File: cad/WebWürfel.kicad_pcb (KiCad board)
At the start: 2 copper layers, 64 x 115 mm, 45 parts, among them K1 1x03, T1 IRF9952, T2 FDN337N, T3 IRLML9301, U1 WeMos_D1_mini, U2 TSR1-2450

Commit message: old led grid
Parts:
- added REF**: MountingHole_3.5mm, MountingHole:MountingHole_3.5mm, F.Cu at (117.5, 52.5)
- added REF**: MountingHole_3.5mm, MountingHole:MountingHole_3.5mm, F.Cu at (149.1, 52.5)
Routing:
- net GND: track 11.5 -> 13.6 mm
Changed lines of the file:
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@@
       (solder_mask_margin 0.1016) (thermal_bridge_angle 45))
+  )
+  (footprint "MountingHole:MountingHole_3.5mm" (layer "F.Cu")
+    (at 117.5 52.5)
+    (descr "Mounting Hole 3.5mm, no annular")
+    (tags "mounting hole 3.5mm no annular")
+    (attr exclude_from_pos_files exclude_from_bom)
+    (fp_text reference "REF**" (at 0 -4.5) (layer "F.SilkS")
+        (effects (font (size 1 1) (thickness 0.15)))
+    )
+    (fp_text value "MountingHole_3.5mm" (at 0 4.4) (layer "F.Fab") hide
+        (effects (font (size 1 1) (thickness 0.15)))
+    )
+    (fp_text user "${REFERENCE}" (at 0 0) (layer "F.Fab")
+        (effects (font (size 1 1) (thickness 0.15)))
+    )
+    (fp_circle (center 0 0) (end 3.5 0)
+      (stroke (width 0.15) (type solid)) (fill none) (layer "Cmts.User"))
+    (fp_circle (center 0 0) (end 3.75 0)
+      (stroke (width 0.05) (type solid)) (fill none) (layer "F.CrtYd"))
+    (pad "" np_thru_hole circle (at 0 0) (size 3.5 3.5) (drill 3.5) (layers "F&B.Cu" "*.Mask"))
   )
   (footprint "D1Mini_Wuerfel_aktuell:WS2812B_9" (layer "F.Cu")
@@
       (rotate (xyz 0 0 0))
     )
+  )
+  (footprint "MountingHole:MountingHole_3.5mm" (layer "F.Cu")
+    (at 149.1 52.5)
+    (descr "Mounting Hole 3.5mm, no annular")
+    (tags "mounting hole 3.5mm no annular")
+    (attr exclude_from_pos_files exclude_from_bom)
+    (fp_text reference "REF**" (at 0 -4.5) (layer "F.SilkS")
+        (effects (font (size 1 1) (thickness 0.15)))
+    )
+    (fp_text value "MountingHole_3.5mm" (at 0 4.5) (layer "F.Fab") hide
+        (effects (font (size 1 1) (thickness 0.15)))
+    )
+    (fp_text user "${REFERENCE}" (at 0 0) (layer "F.Fab")
+        (effects (font (size 1 1) (thickness 0.15)))
+    )
+    (fp_circle (center 0 0) (end 3.5 0)
+      (stroke (width 0.15) (type solid)) (fill none) (layer "Cmts.User"))
+    (fp_circle (center 0 0) (end 3.75 0)
+      (stroke (width 0.05) (type solid)) (fill none) (layer "F.CrtYd"))
+    (pad "" np_thru_hole circle (at 0 0) (size 3.5 3.5) (drill 3.5) (layers "*.Cu" "*.Mask"))
   )
   (footprint "D1Mini_Wuerfel_aktuell:WS2812B_9" (layer "F.Cu")
@@
     (pad "" np_thru_hole circle (at 0 0 180) (size 2.5 2.5) (drill 2.5) (layers "*.Cu" "*.Mask"))
   )
-  (gr_line (start 117.25 147.75) (end 117.25 150.75)
-    (stroke (width 0.4) (type default)) (layer "F.SilkS"))
-  (gr_line (start 122.75 138.25) (end 122.75 133.5)
-    (stroke (width 0.4) (type default)) (layer "F.SilkS"))
-  (gr_line (start 107.5 121.5) (end 107.5 127.25)
-    (stroke (width 1) (type default)) (layer "F.SilkS"))
-  (gr_line (start 134.75 135.5) (end 134.75 144)
-    (stroke (width 0.4) (type default)) (layer "F.SilkS"))
   (gr_line (start 101.29 155) (end 165.29 155)
     (stroke (width 0.3) (type solid)) (layer "Edge.Cuts"))
@@
   (gr_line (start 165.29 155) (end 165.29 40)
     (stroke (width 0.3) (type solid)) (layer "Edge.Cuts"))
+  (segment (start 108.458 112.014) (end 108.458 111.998) (width 2) (layer "F.Cu") (net 1))
   (segment (start 124.845 137.77) (end 125.365 137.25) (width 0.3) (layer "F.Cu") (net 1))
   (segment (start 128.25 137.25) (end 128.75 136.75) (width 0.3) (layer "F.Cu") (net 1))
   (segment (start 125.365 137.25) (end 128.25 137.25) (width 0.3) (layer "F.Cu") (net 1))
+  (segment (start 107 110.54) (end 108.458 111.998) (width 2) (layer "F.Cu") (net 1))
   (segment (start 124.845 139.2) (end 124.845 137.77) (width 0.3) (layer "F.Cu") (net 1))
   (via (at 107.5 127.25) (size 2) (drill 1.2) (layers "F.Cu" "B.Cu") (free) (net 1))
@@
   (zone (net 1) (net_name "GND") (layer "F.Cu") (name "GND_1") (hatch edge 0.5)
     (priority 2)
-    (connect_pads yes (clearance 0.5))
+    (connect_pads (clearance 0.5))
     (min_thickness 0.25) (filled_areas_thickness no)
     (fill yes (thermal_gap 0.5) (thermal_bridge_width 0.5) (smoothing fillet) (radius 1))
@@
         (xy 114.25 101.75)
         (xy 114.25 104)
-        (xy 160.5 104)
-        (xy 160.5 61.75)
+        (xy 158.95 104.013)
+        (xy 158.95 61.73)
       )
     )
@@
   (zone (net 1) (net_name "GND") (layer "F.Cu") (name "GND_0") (hatch edge 0.5)
     (priority 1)
-    (connect_pads yes (clearance 1.3))
+    (connect_pads (clearance 1.3))
     (min_thickness 0.25) (filled_areas_thickness no)
     (fill yes (thermal_gap 0.5) (thermal_bridge_width 0.5) (smoothing chamfer) (radius 1.3))
@@
       )
     )
+  )
+  (zone (net 1) (net_name "GND") (layer "F.Cu") (name "GND_3") (hatch edge 0.5)
+    (priority 3)
+    (connect_pads yes (clearance 1.3))
+    (min_thickness 0.25) (filled_areas_thickness no)
+    (fill yes (thermal_gap 0.5) (thermal_bridge_width 0.5) (smoothing chamfer) (radius 1.3))
+    (polygon
+      (pts
+        (xy 144.145 129.032)
+        (xy 144.145 130.175)
+        (xy 145.923 130.175)
+        (xy 145.923 129.032)
+      )
+    )
+  )
+  (zone (net 1) (net_name "GND") (layer "F.Cu") (name "GND4") (hatch edge 0.5)
+    (priority 3)
+    (connect_pads yes (clearance 1.3))
+    (min_thickness 0.25) (filled_areas_thickness no)
+    (fill yes (thermal_gap 0.5) (thermal_bridge_width 0.5))
+    (polygon
+      (pts
+        (xy 112.014 130.302)
+        (xy 112.014 132.08)
+        (xy 113.665 132.08)
+        (xy 113.665 130.302)
+      )
+    )

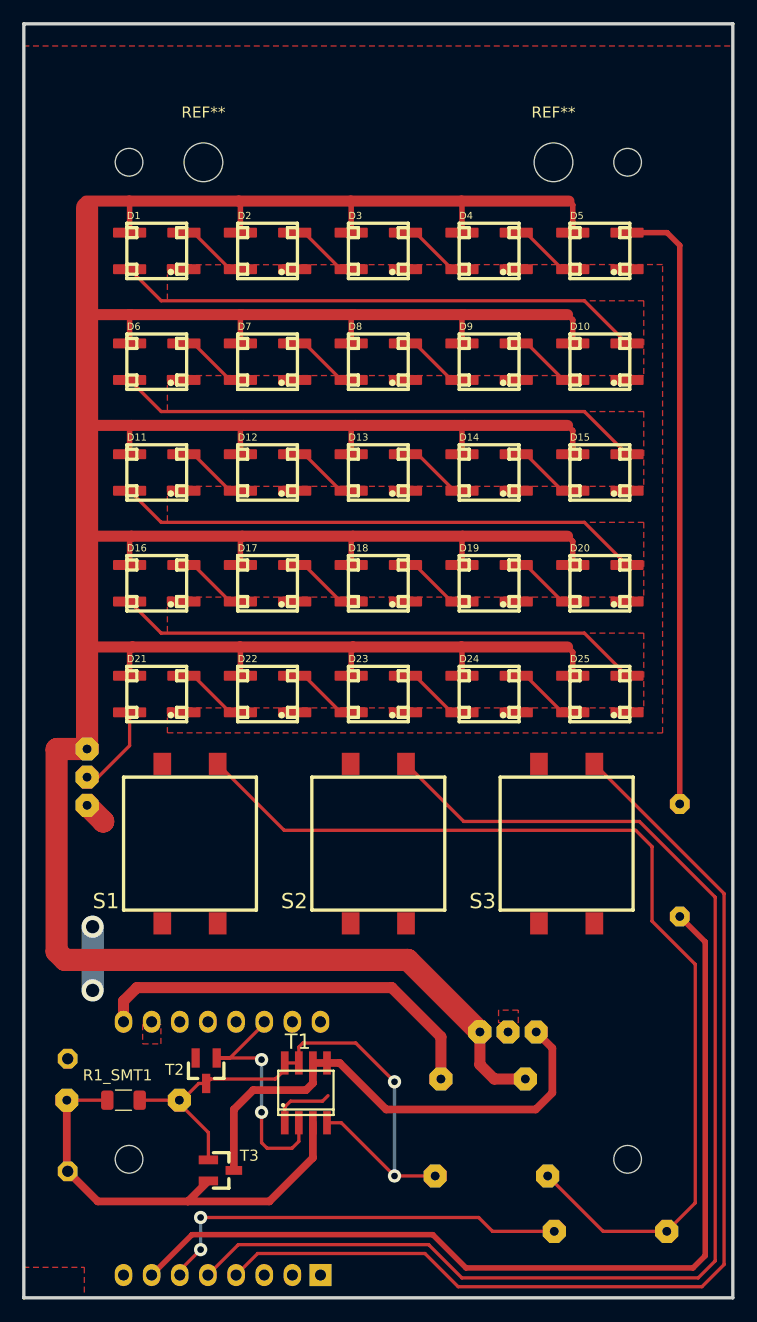
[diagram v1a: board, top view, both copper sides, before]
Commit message: rotated d1 mini by 90°
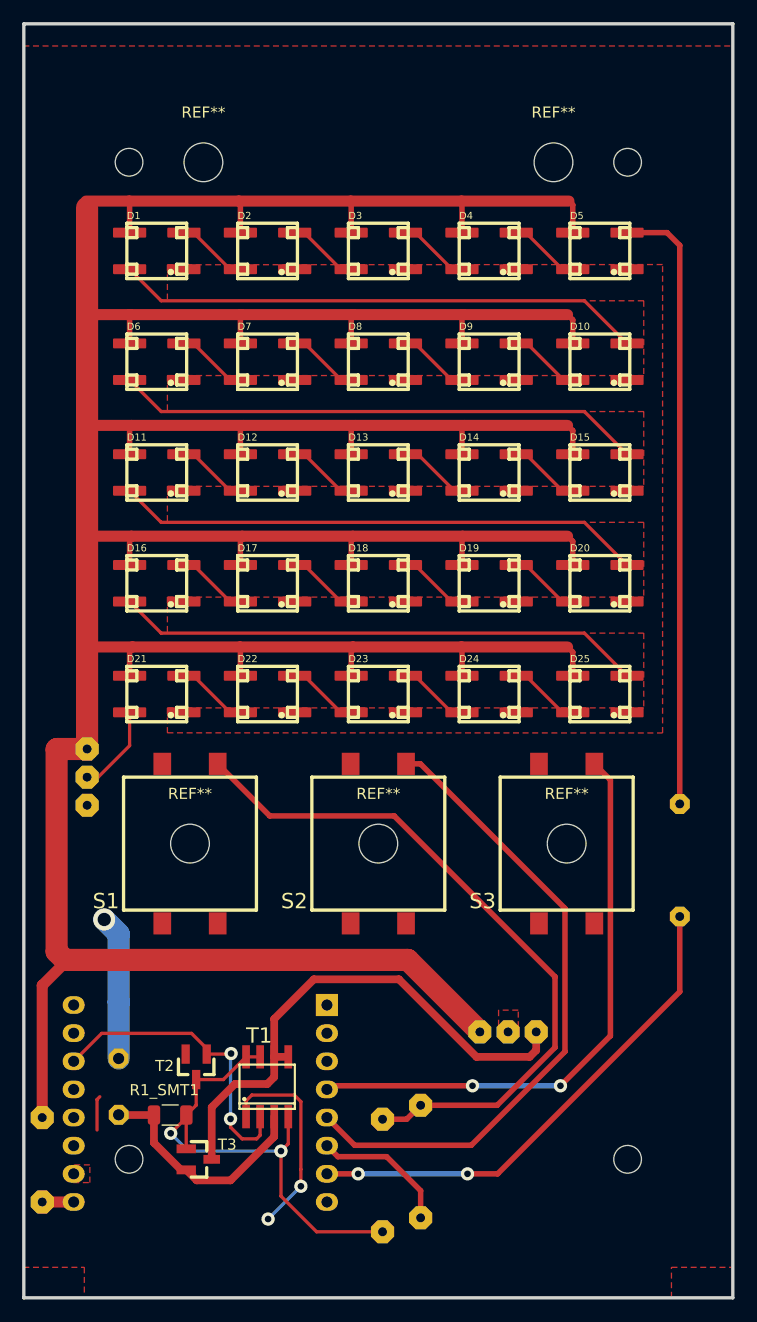
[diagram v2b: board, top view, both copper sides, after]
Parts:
- removed R1_THT1: 100K, D1Mini_Wuerfel_aktuell:0207_37
- added REF**: MountingHole_3.5mm, MountingHole:MountingHole_3.5mm, F.Cu at (116.3, 114.0)
- added REF**: MountingHole_3.5mm, MountingHole:MountingHole_3.5mm, F.Cu at (150.3, 114.0)
- added REF**: MountingHole_3.5mm, MountingHole:MountingHole_3.5mm, F.Cu at (133.3, 114.0)
- moved D26 40.5 mm to (103.0, 142.5), turned to -90 degrees
- moved U1 24.4 mm to (128.7, 128.6), turned to 180 degrees
- moved D28 18.3 mm to (137.1, 142.7), turned to 90 degrees
- moved D27 9.83 mm to (133.7, 144.0), turned to 90 degrees
- moved BAT1 4.60 mm to (109.8, 141.0)
- moved R1_SMT1 4.42 mm to (114.5, 138.5)
- moved T1 3.54 mm to (123.3, 135.9)
- moved T3 2.24 mm to (117.1, 142.5)
- moved T2 0.97 mm to (116.8, 134.2)
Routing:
- net /D6: track 114.5 -> 58.7 mm
- net /D5: track 97.0 -> 52.7 mm, vias 0 -> 2
- net /D8: track 84.8 -> 45.4 mm, vias 0 -> 2
- net +5VD: track 36.7 -> 2.84 mm
- net Net-(D27-Pad2): track 92.5 -> 63.0 mm
- net /D7: track 38.4 -> 12.6 mm, vias 2 -> 0
- net GND: track 13.6 -> 35.0 mm, vias 2 -> 3
- net +9V: track 39.9 -> 21.4 mm
- net XFET: track 54.5 -> 44.0 mm
- net +5V: track 407.9 -> 415.4 mm
- net D1: track 22.9 -> 27.9 mm
- net U2_VIN: track 45.5 -> 47.9 mm

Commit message: kicad update battery
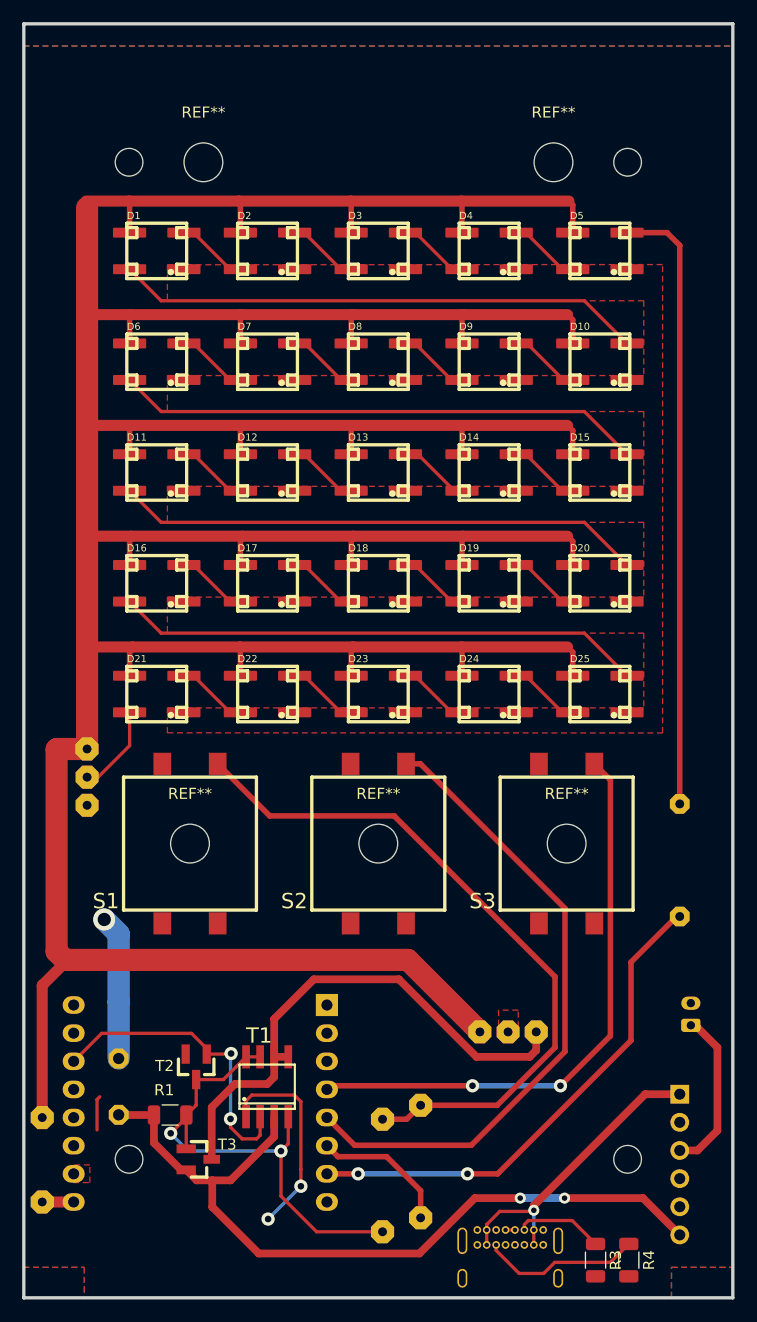
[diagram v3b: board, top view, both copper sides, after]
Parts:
- added J1: Conn_01x06, Connector_PinHeader_2.54mm:PinHeader_1x06_P2.54mm_Vertical, B.Cu at (160.5, 136.6)
- added J2: Conn_01x02, Connector_JST:JST_PH_B2B-PH-K_1x02_P2.00mm_Vertical, B.Cu at (161.5, 130.4)
- added P1: USB_C_Plug_USB2.0, Connector_USB:USB_C_Receptacle_GCT_USB4085, B.Cu at (148.2, 148.9)
- added R3: 5.1K, Resistor_SMD:R_1206_3216Metric, F.Cu at (152.9, 151.6)
- added R4: 5.1K, Resistor_SMD:R_1206_3216Metric, F.Cu at (155.9, 151.6)
- renumbered R1_SMT1 to R1
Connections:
- net +9V renamed VCC
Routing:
- net VCC: track 21.4 -> 71.2 mm, vias 0 -> 2
- net VBUS: track 0.00 -> 27.5 mm, vias 0 -> 1
- net +BATT: track 0.00 -> 14.9 mm
- net Net-(P1-VCONN): track 0.00 -> 14.4 mm
- net Net-(P1-CC): track 0.00 -> 7.94 mm
- net Net-(P1-D+): track 0.00 -> 0.85 mm
- added copper zone on B.Cu, net GND
